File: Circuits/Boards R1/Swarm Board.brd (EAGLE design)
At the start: 63.5 x 63.5 mm, 89 parts, among them CON1 ISP(2X3), T1 NPN2N2222, T10 TEFT4300, T13 NPN2N2222, T14 NPN2N2222, T15 NPN2N2222, T16 NPN2N2222, T17 NPN2N2222, T18 NPN2N2222, T2 NPN2N2222, T3 NPN2N2222, T4 TEFT4300, T5 TEFT4300, T6 TEFT4300, T7 TEFT4300, T8 TEFT4300, T9 TEFT4300, U1 ATMEGA324P, U2 MCP73832SOT-23, U3 TB6552FN/FNG

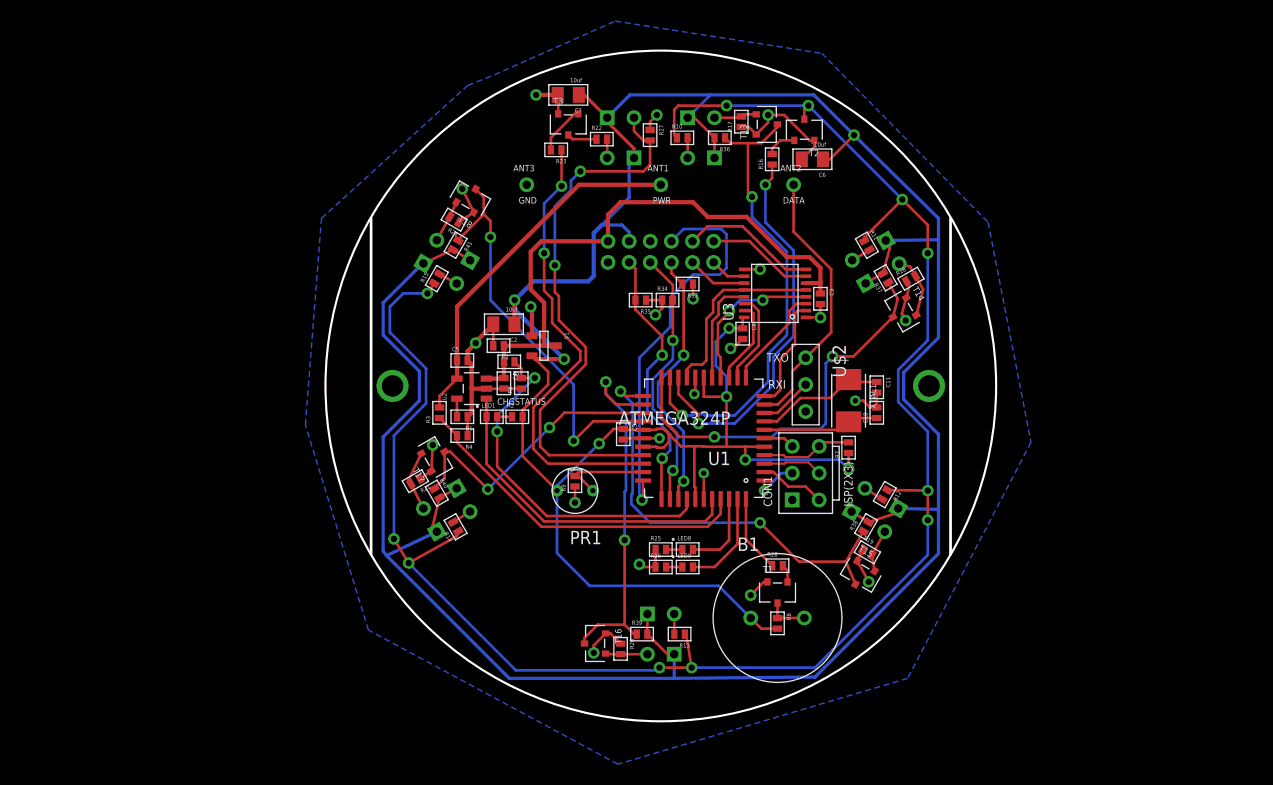
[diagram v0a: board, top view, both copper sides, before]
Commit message: 
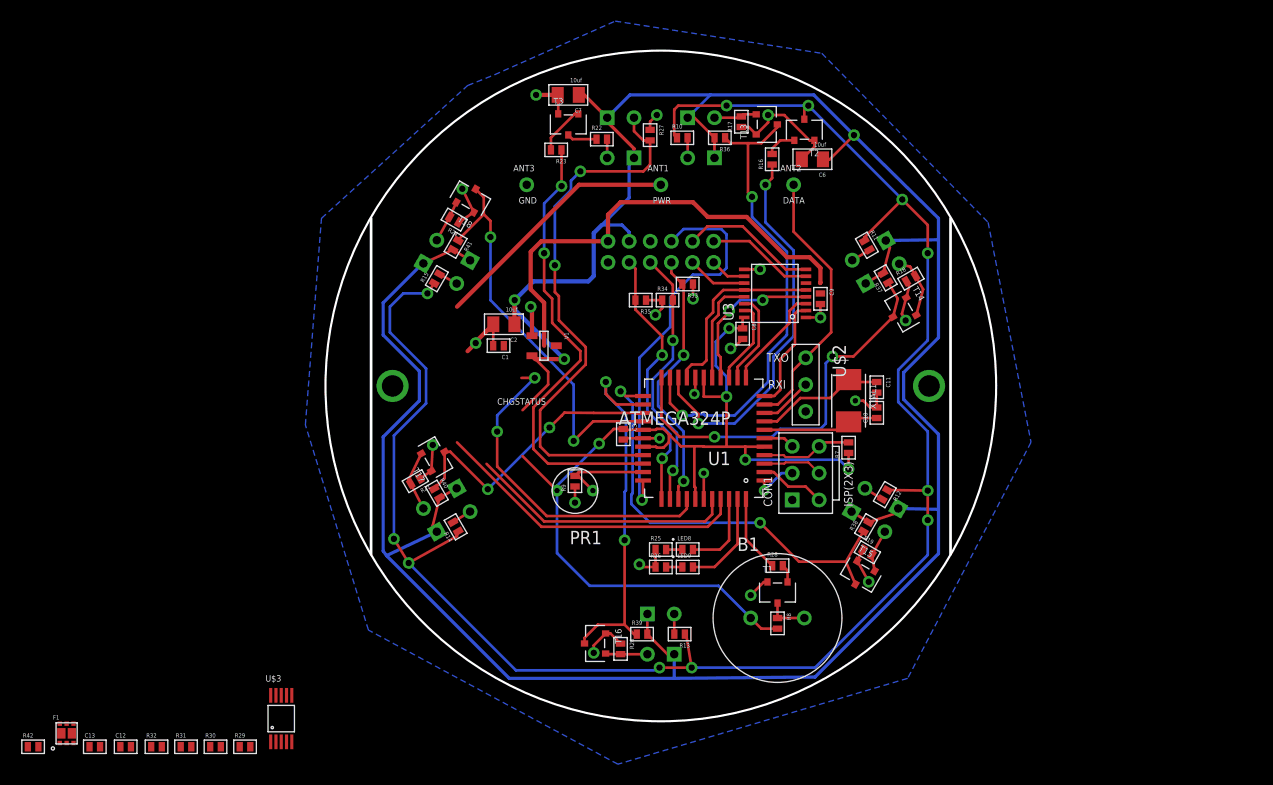
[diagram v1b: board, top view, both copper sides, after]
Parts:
- removed C4, C5: 4.7uf, Passive:0603
- removed LED1: red, Passive:LED0603
- removed R1, R3: 2k, Passive:0603
- removed R2: 750, Passive:0603
- removed R4: 3k, Passive:0603
- removed R5: 7k, Passive:0603
- removed R6: 18k, Passive:0603
- removed U2: MCP73832SOT-23, PowerIC:(OT)SOT-23(5PAD)
- added C12, C13: 4.7uf, Passive:0603
- added F1: FDFMA2P857, Passive:MICROFET2X2MM
- added R29: 7k, Passive:0603
- added R30: 18k, Passive:0603
- added R31, R42: 10k, Passive:0603
- added R32: 2k, Passive:0603
- added U$3: MCP73833, PowerIC:MSOP10
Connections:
- removed net N$1: R1.2, U2.5
- removed net N$4: LED1.2, R2.1
- new net +VRAW: C1.1, C9.1, F1.4, F1.6, F1.7, U3.6, V1.3
- new net N$22: R31.2, U$3.8
- new net N$28: R32.2, U$3.6
- new net N$31: U$3.10, U$3.9
- new net N$33: U$3.3
- net +3V: no longer R2.2
- net +VBAT: now also C13.1, F1.3, F1.8, R29.2; no longer C1.1, C4.1, C9.1, R5.2, U2.3, U3.6, V1.3
- net +VCHG: now also C12.1, F1.1, F1.5, R42.2, U$3.1, U$3.2; no longer C5.1, R3.2, U2.4
- net CHGDETECT: now also U$3.7; no longer R3.1, R4.2
- net CHGSTATUS: now also U$3.4; no longer LED1.1, U2.1
- net GND: now also C12.2, C13.2, R30.1, R31.1, R32.1, R42.1, U$3.5; no longer C4.2, C5.2, R1.1, R4.1, R6.1, U2.2
- net VSENSE: now also R29.1, R30.2; no longer R5.1, R6.2
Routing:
- net GND: track 89.8 -> 76.8 mm
- net +VBAT: track 56.4 -> 44.3 mm
- net +VCHG: track 34.3 -> 24.1 mm
- net CHGSTATUS: track 31.5 -> 25.4 mm
- net +3V: track 375.0 -> 370.7 mm
- net CHGDETECT: track 33.2 -> 30.2 mm
- net VSENSE: track 34.0 -> 32.2 mm
- net N$1: track 1.72 -> 0.00 mm
- net N$4: track 1.41 -> 0.00 mm

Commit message: changed charge circuit to incorporate mcp73833 and p-fet/diode for ppm
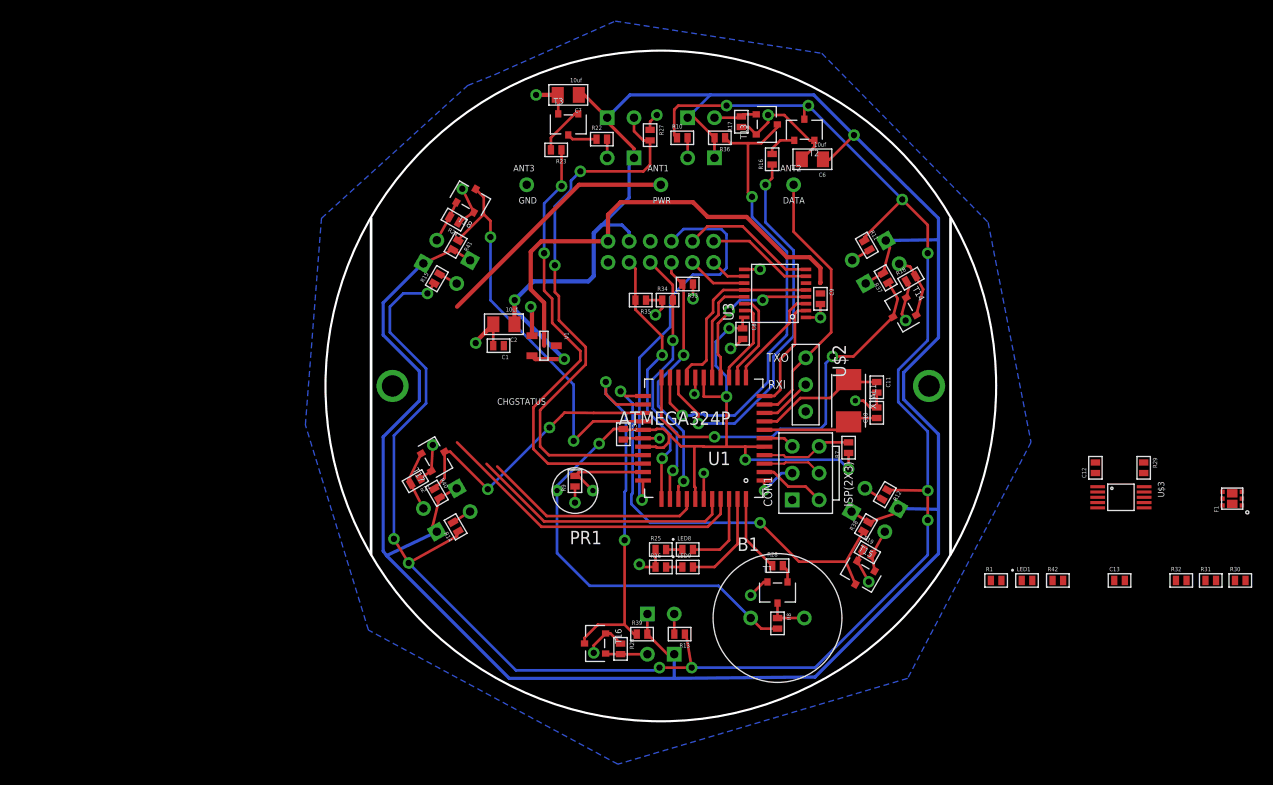
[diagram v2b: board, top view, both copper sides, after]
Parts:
- added LED1: (no value), Passive:LED0603
- added R1: (no value), Passive:0603
- moved F1 112.6 mm to (85.9, 21.1), turned to 90 degrees
- moved R30 98.3 mm to (86.6, 13.3)
- moved C13 98.3 mm to (75.2, 13.3)
- moved R31 98.3 mm to (83.8, 13.3)
- moved R32 98.3 mm to (81.0, 13.3)
- moved R42 98.3 mm to (69.3, 13.3)
- moved C12 95.5 mm to (72.9, 24.0), turned to 90 degrees
- moved R29 89.1 mm to (77.5, 24.0), turned to 270 degrees
- moved U$3 82.2 mm to (75.3, 21.2), turned to 270 degrees
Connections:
- removed net N$31: U$3.10, U$3.9
- new net N$1: LED1.1, R1.2
- net +VBAT: now also U$3.10, U$3.9
- net +VCHG: now also LED1.2
- net N$33: now also R1.1
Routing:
- net +3V: track 370.7 -> 359.3 mm
- net VSENSE: track 32.2 -> 21.1 mm, vias 2 -> 0
- net GND: track 76.8 -> 75.7 mm

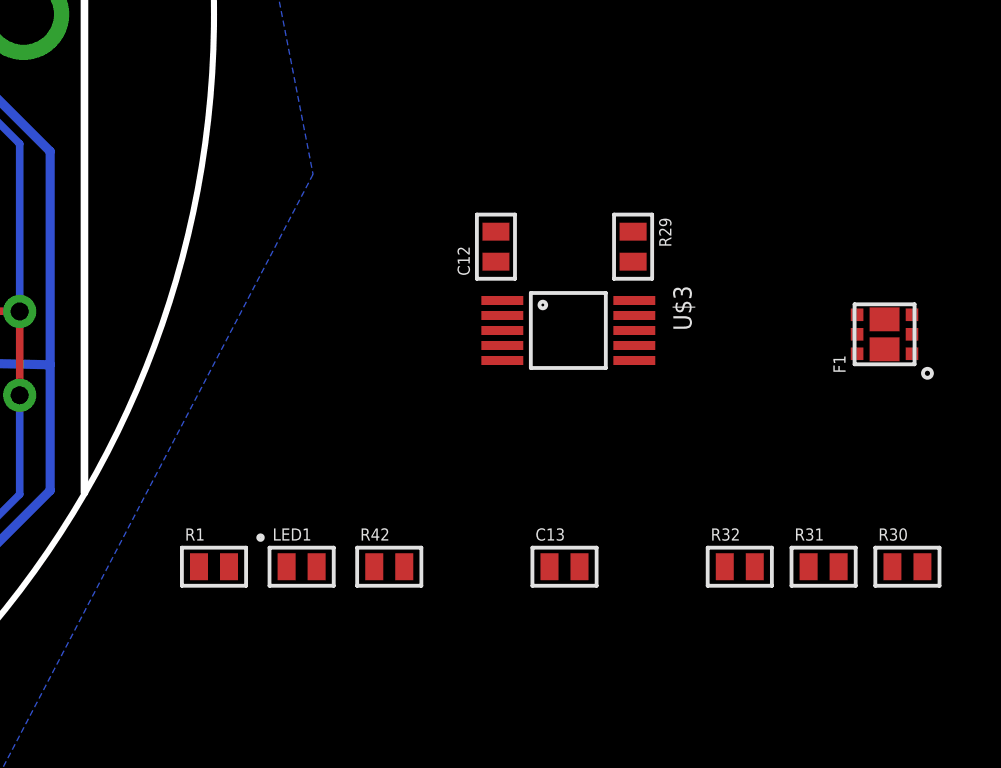
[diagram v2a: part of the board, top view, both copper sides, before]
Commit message: 
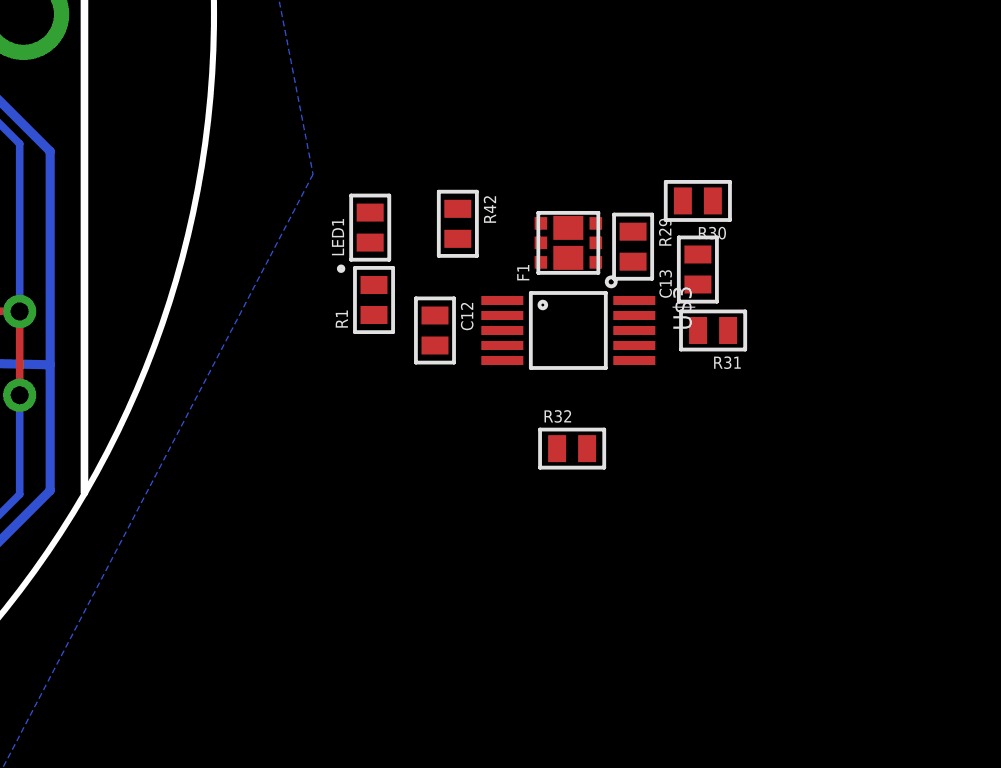
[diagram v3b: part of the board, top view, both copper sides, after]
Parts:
- LED1: value (none) -> red
- moved R30 14.1 mm to (79.6, 25.5), turned to 180 degrees
- moved R42 11.7 mm to (71.6, 24.8), turned to 270 degrees
- moved LED1 11.5 mm to (68.7, 24.6), turned to 90 degrees
- moved F1 11.0 mm to (75.3, 24.1)
- moved C13 10.9 mm to (79.6, 23.2), turned to 90 degrees
- moved R1 10.4 mm to (68.8, 22.2), turned to 90 degrees
- moved R31 8.69 mm to (80.1, 21.2), turned to 180 degrees
- moved R32 6.84 mm to (75.4, 17.3)
- moved C12 3.45 mm to (70.9, 21.2), turned to 270 degrees
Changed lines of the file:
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@@
 <element name="U$3" library="PowerIC" package="MSOP10" value="MCP73833" x="75.311" y="21.209" rot="R270"/>
 <element name="R29" library="Passive" package="0603" value="7k" x="77.47" y="24.003" rot="R270"/>
-<element name="R30" library="Passive" package="0603" value="18k" x="86.614" y="13.335"/>
-<element name="R31" library="Passive" package="0603" value="10k" x="83.82" y="13.335"/>
-<element name="R32" library="Passive" package="0603" value="2k" x="81.026" y="13.335"/>
-<element name="C12" library="Passive" package="0603" value="4.7uf" x="72.898" y="24.003" rot="R90"/>
-<element name="C13" library="Passive" package="0603" value="4.7uf" x="75.184" y="13.335"/>
-<element name="F1" library="Passive" package="MICROFET2X2MM" value="FDFMA2P857" x="85.852" y="21.082" rot="R90"/>
-<element name="R42" library="Passive" package="0603" value="10k" x="69.342" y="13.335"/>
-<element name="LED1" library="Passive" package="LED0603" value="" x="66.421" y="13.335"/>
-<element name="R1" library="Passive" package="0603" value="" x="63.5" y="13.335"/>
+<element name="R30" library="Passive" package="0603" value="18k" x="79.629" y="25.527" rot="R180"/>
+<element name="R31" library="Passive" package="0603" value="10k" x="80.137" y="21.209" rot="R180"/>
+<element name="R32" library="Passive" package="0603" value="2k" x="75.438" y="17.272"/>
+<element name="C12" library="Passive" package="0603" value="4.7uf" x="70.866" y="21.209" rot="R270"/>
+<element name="C13" library="Passive" package="0603" value="4.7uf" x="79.629" y="23.241" rot="R90"/>
+<element name="F1" library="Passive" package="MICROFET2X2MM" value="FDFMA2P857" x="75.311" y="24.13" rot="R90"/>
+<element name="R42" library="Passive" package="0603" value="10k" x="71.628" y="24.765" rot="R270"/>
+<element name="LED1" library="Passive" package="LED0603" value="red" x="68.707" y="24.638" rot="R90"/>
+<element name="R1" library="Passive" package="0603" value="" x="68.834" y="22.225" rot="R90"/>
 </elements>
 <signals>
@@
 <contactref element="R31" pad="1"/>
 <contactref element="R42" pad="1"/>
-<wire x1="75.684" y1="13.335" x2="68.842" y2="13.335" width="0" layer="19" extent="1-1"/>
-<wire x1="72.898" y1="24.503" x2="75.684" y2="13.335" width="0" layer="19" extent="1-1"/>
-<wire x1="80.526" y1="13.335" x2="72.898" y2="24.503" width="0" layer="19" extent="1-1"/>
-<wire x1="83.32" y1="13.335" x2="80.526" y2="13.335" width="0" layer="19" extent="1-1"/>
-<wire x1="86.114" y1="13.335" x2="83.32" y2="13.335" width="0" layer="19" extent="1-1"/>
-<wire x1="73.111" y1="20.209" x2="86.114" y2="13.335" width="0" layer="19" extent="1-1"/>
-<wire x1="8.9420125" y1="22.983" x2="73.111" y2="20.209" width="0" layer="19" extent="1-1"/>
+<wire x1="79.629" y1="23.741" x2="80.129" y2="25.527" width="0" layer="19" extent="1-1"/>
+<wire x1="80.637" y1="21.209" x2="79.629" y2="23.741" width="0" layer="19" extent="1-1"/>
+<wire x1="74.938" y1="17.272" x2="80.637" y2="21.209" width="0" layer="19" extent="1-1"/>
+<wire x1="73.111" y1="20.209" x2="74.938" y2="17.272" width="0" layer="19" extent="1-1"/>
+<wire x1="70.866" y1="20.709" x2="73.111" y2="20.209" width="0" layer="19" extent="1-1"/>
+<wire x1="71.628" y1="25.265" x2="70.866" y2="20.709" width="0" layer="19" extent="1-1"/>
+<wire x1="52.197" y1="29.71" x2="71.628" y2="25.265" width="0" layer="19" extent="1-1"/>
 </signal>
 <signal name="+VBAT">
@@
 <contactref element="U$3" pad="10"/>
 <contactref element="U$3" pad="9"/>
-<wire x1="77.511" y1="21.709" x2="20.701" y2="35.56" width="0" layer="19" extent="1-1"/>
-<wire x1="77.511" y1="22.209" x2="77.511" y2="21.709" width="0" layer="19" extent="1-1"/>
-<wire x1="77.47" y1="23.503" x2="77.511" y2="22.209" width="0" layer="19" extent="1-1"/>
-<wire x1="74.684" y1="13.335" x2="77.47" y2="23.503" width="0" layer="19" extent="1-1"/>
-<wire x1="86.767" y1="21.732" x2="74.684" y2="13.335" width="0" layer="19" extent="1-1"/>
-<wire x1="85.852" y1="21.582" x2="86.767" y2="21.732" width="0" layer="19" extent="1-1"/>
+<wire x1="77.511" y1="22.209" x2="77.47" y2="23.503" width="0" layer="19" extent="1-1"/>
+<wire x1="77.511" y1="21.709" x2="77.511" y2="22.209" width="0" layer="19" extent="1-1"/>
+<wire x1="76.226" y1="24.78" x2="77.47" y2="23.503" width="0" layer="19" extent="1-1"/>
+<wire x1="75.311" y1="24.63" x2="76.226" y2="24.78" width="0" layer="19" extent="1-1"/>
+<wire x1="79.629" y1="22.741" x2="77.511" y2="22.209" width="0" layer="19" extent="1-1"/>
+<wire x1="46.863" y1="41.529" x2="75.311" y2="24.63" width="0" layer="19" extent="1-1"/>
 </signal>
 <signal name="+VCHG">
@@
 <contactref element="R42" pad="2"/>
 <contactref element="LED1" pad="2"/>
-<wire x1="73.111" y1="21.709" x2="12.454" y2="39.251" width="0" layer="19" extent="1-1"/>
-<wire x1="73.111" y1="22.209" x2="73.111" y2="21.709" width="0" layer="19" extent="1-1"/>
-<wire x1="72.898" y1="23.503" x2="73.111" y2="22.209" width="0" layer="19" extent="1-1"/>
-<wire x1="84.937" y1="21.082" x2="72.898" y2="23.503" width="0" layer="19" extent="1-1"/>
-<wire x1="86.767" y1="20.432" x2="84.937" y2="21.082" width="0" layer="19" extent="1-1"/>
-<wire x1="69.842" y1="13.335" x2="86.767" y2="20.432" width="0" layer="19" extent="1-1"/>
-<wire x1="66.921" y1="13.335" x2="69.842" y2="13.335" width="0" layer="19" extent="1-1"/>
+<wire x1="74.396" y1="24.13" x2="76.226" y2="23.48" width="0" layer="19" extent="1-1"/>
+<wire x1="73.111" y1="22.209" x2="74.396" y2="24.13" width="0" layer="19" extent="1-1"/>
+<wire x1="73.111" y1="21.709" x2="73.111" y2="22.209" width="0" layer="19" extent="1-1"/>
+<wire x1="70.866" y1="21.709" x2="73.111" y2="21.709" width="0" layer="19" extent="1-1"/>
+<wire x1="71.628" y1="24.265" x2="73.111" y2="22.209" width="0" layer="19" extent="1-1"/>
+<wire x1="68.707" y1="25.138" x2="71.628" y2="24.265" width="0" layer="19" extent="1-1"/>
+<wire x1="31.75" y1="50.8" x2="68.707" y2="25.138" width="0" layer="19" extent="1-1"/>
 </signal>
 <signal name="CHGDETECT">
@@
 <wire x1="37.414" y1="19.634" x2="37.414" y2="21.047" width="0.254" layer="1"/>
 <contactref element="U$3" pad="7"/>
-<wire x1="77.511" y1="20.709" x2="12.454" y2="26.408" width="0" layer="19" extent="1-1"/>
+<wire x1="37.414" y1="21.047" x2="77.511" y2="20.709" width="0" layer="19" extent="1-1"/>
 </signal>
 <signal name="VSENSE">
@@
 <contactref element="R29" pad="1"/>
 <contactref element="R30" pad="2"/>
-<wire x1="77.47" y1="24.503" x2="16.256" y2="24.13" width="0" layer="19" extent="1-1"/>
-<wire x1="87.114" y1="13.335" x2="77.47" y2="24.503" width="0" layer="19" extent="1-1"/>
+<wire x1="77.47" y1="24.503" x2="79.129" y2="25.527" width="0" layer="19" extent="1-1"/>
+<wire x1="34.214" y1="21.047" x2="77.47" y2="24.503" width="0" layer="19" extent="1-1"/>
 </signal>
 <signal name="N$2">
@@
 <wire x1="20.701" y1="18.923" x2="15.248" y2="24.376" width="0.254" layer="1"/>
 <contactref element="U$3" pad="4"/>
-<wire x1="73.111" y1="20.709" x2="20.701" y2="18.923" width="0" layer="19" extent="1-1"/>
+<wire x1="36.614" y1="21.047" x2="73.111" y2="20.709" width="0" layer="19" extent="1-1"/>
 </signal>
 <signal name="DISTANCERECEIVE">
@@
 <contactref element="U$3" pad="6"/>
 <contactref element="R32" pad="2"/>
-<wire x1="77.511" y1="20.209" x2="81.526" y2="13.335" width="0" layer="19" extent="1-1"/>
+<wire x1="75.938" y1="17.272" x2="77.511" y2="20.209" width="0" layer="19" extent="1-1"/>
 </signal>
 <signal name="N$33">
 <contactref element="U$3" pad="3"/>
 <contactref element="R1" pad="1"/>
-<wire x1="73.111" y1="21.209" x2="63" y2="13.335" width="0" layer="19" extent="1-1"/>
+<wire x1="68.834" y1="21.725" x2="73.111" y2="21.209" width="0" layer="19" extent="1-1"/>
 </signal>
 <signal name="N$22">
 <contactref element="U$3" pad="8"/>
 <contactref element="R31" pad="2"/>
-<wire x1="77.511" y1="21.209" x2="84.32" y2="13.335" width="0" layer="19" extent="1-1"/>
+<wire x1="77.511" y1="21.209" x2="79.637" y2="21.209" width="0" layer="19" extent="1-1"/>
 </signal>
 <signal name="+VRAW">
@@
 <contactref element="U3" pad="6"/>
 <contactref element="C9" pad="1"/>
-<wire x1="46.863" y1="40.505" x2="45.495" y2="41.488" width="0" layer="19" extent="1-1"/>
+<wire x1="74.396" y1="23.48" x2="75.311" y2="23.63" width="0" layer="19" extent="1-1"/>
+<wire x1="74.396" y1="24.78" x2="74.396" y2="23.48" width="0" layer="19" extent="1-1"/>
+<wire x1="46.863" y1="40.505" x2="74.396" y2="24.78" width="0" layer="19" extent="1-1"/>
+<wire x1="45.495" y1="41.488" x2="46.863" y2="40.505" width="0" layer="19" extent="1-1"/>
 <wire x1="21.851" y1="35.56" x2="45.495" y2="41.488" width="0" layer="19" extent="1-1"/>
 <wire x1="16.883" y1="35.56" x2="21.851" y2="35.56" width="0" layer="19" extent="1-1"/>
-<wire x1="84.937" y1="21.732" x2="16.883" y2="35.56" width="0" layer="19" extent="1-1"/>
-<wire x1="84.937" y1="20.432" x2="84.937" y2="21.732" width="0" layer="19" extent="1-1"/>
-<wire x1="85.852" y1="20.582" x2="84.937" y2="20.432" width="0" layer="19" extent="1-1"/>
 </signal>
 <signal name="N$1">
 <contactref element="R1" pad="2"/>
 <contactref element="LED1" pad="1"/>
-<wire x1="65.921" y1="13.335" x2="64" y2="13.335" width="0" layer="19" extent="1-1"/>
+<wire x1="68.834" y1="22.725" x2="68.707" y2="24.138" width="0" layer="19" extent="1-1"/>
 </signal>
 </signals>
